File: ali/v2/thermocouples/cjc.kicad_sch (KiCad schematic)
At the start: 23 parts, among them U10 TMP117AIDRVR, U11 TMP117AIDRVR, U12 TMP117AIDRVR, U13 TMP117AIDRVR, U7 TCA9543A, U8 TMP117AIDRVR, U9 TMP117AIDRVR

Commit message: Globally remove LCSC labels, update MPNs and IOCs, add +5V monitoring to DAQs, fix some footprints
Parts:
- U7: footprint Package_SO:Texas_HTSSOP-14-1EP_4.4x5mm_P0.65mm_EP3.4x5mm_Mask3.155x3.255mm_ThermalVias -> APRL_Package:TSSOP-14_4.4x5mm_P0.65mm; MPN TCA9543A -> TCA9543APWR
- renumbered R44 to R46, R45 to R47, R46 to R48, R47 to R49, R48 to R50, R49 to R51, R50 to R52, R51 to R53, R52 to R54
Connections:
- net GND: no longer U7.15 (GND)

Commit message: Small documentation
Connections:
- net at R50.2: now also U7.8 (~{INT1}); no longer U7.4 (~{INT0})
- net at R49.2: now also U7.4 (~{INT0}); no longer U7.8 (~{INT1})
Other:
- note added: "I2C MUX"
- note added: "SENSORS"
- note removed: "this symbol is off the ints are supposed to be for each input then the big ~{int} is supposed to feed to mcu"
- moved on the sheet: C55, C56, C57, C58, C59, C60, C61, R51, R52, R53, R54, U10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

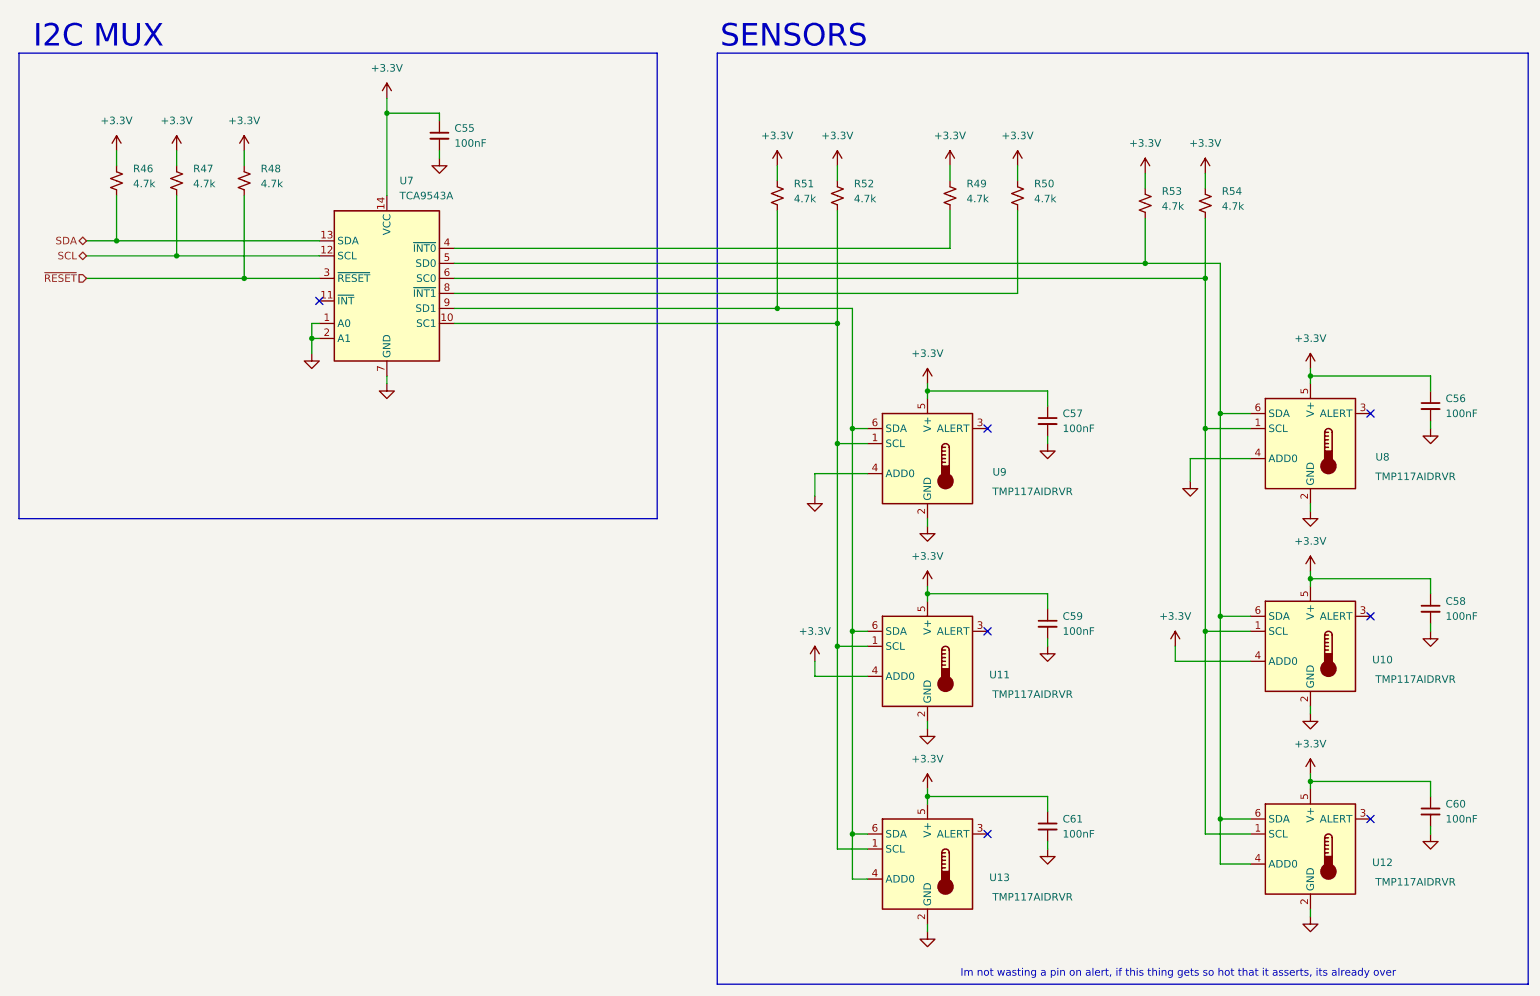
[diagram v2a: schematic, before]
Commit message: the great flatpak and kicad 10.0.6 migration
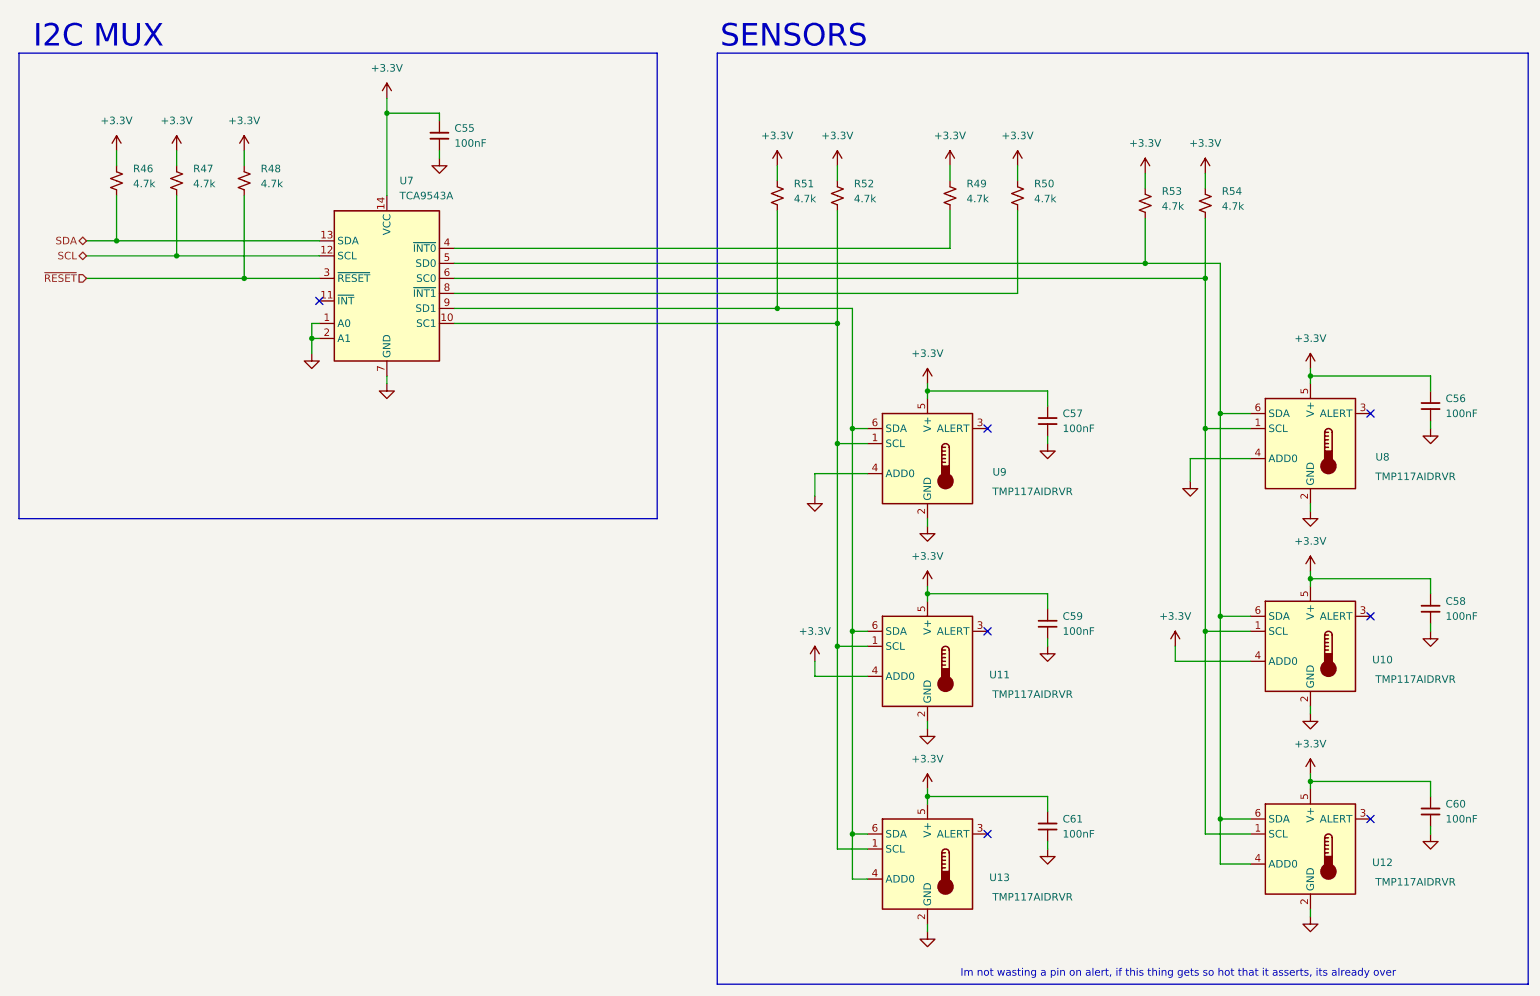
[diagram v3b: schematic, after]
